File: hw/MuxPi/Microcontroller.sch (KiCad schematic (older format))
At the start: 34 parts, among them P1 DS1021-1*6SF1-1, SW1 DTSM-62N-V-B, SW2 DTSM-62N-V-B, U1 STM32F030C6T6, U3 OLED-AG-128032DY-Y (YELLOW), Y1 ABM3B-8.000MHZ-10-1-U-T

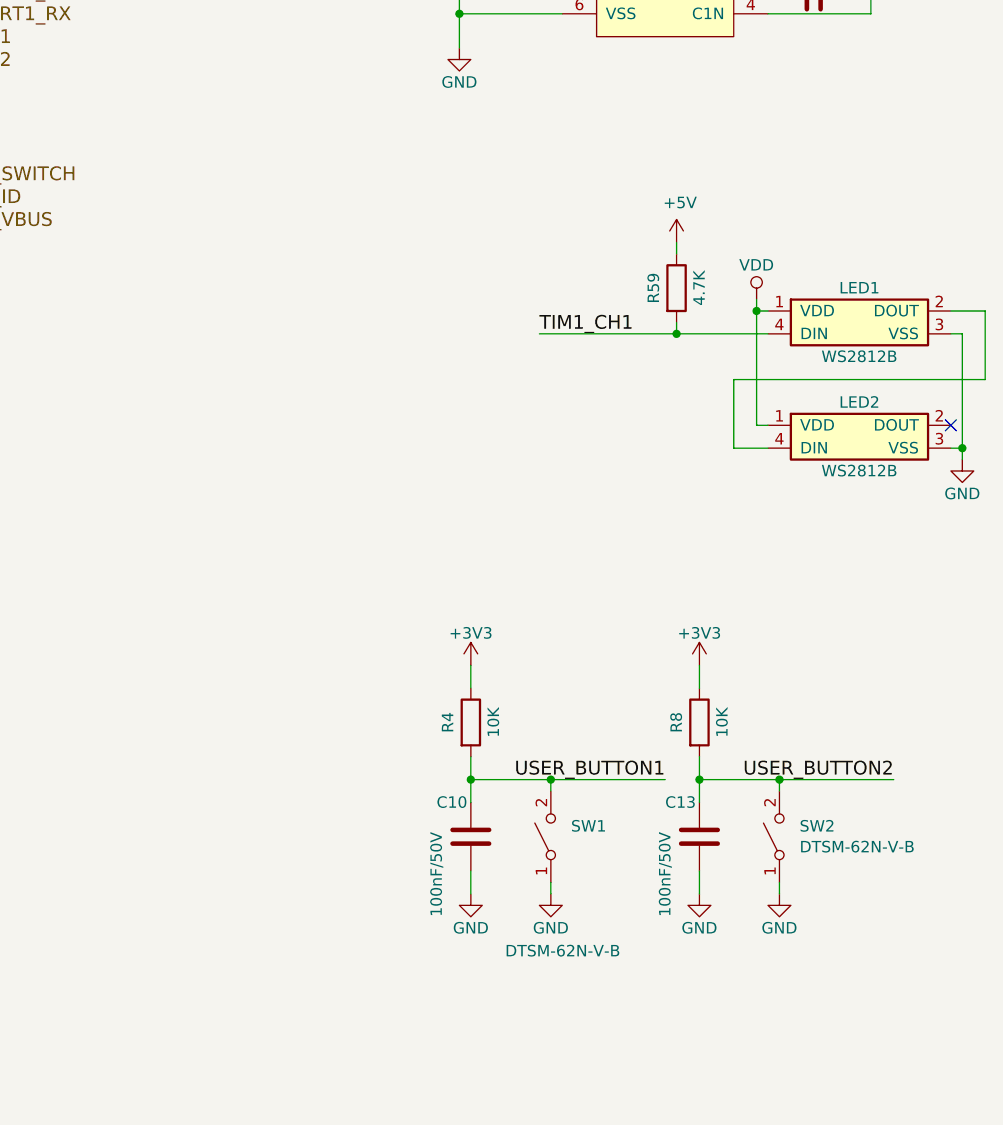
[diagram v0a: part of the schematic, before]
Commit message: Add detailed info to MuxPi electronic components
The additional information includes manufacturer names and
manufacturer symbols for all components except ceramic capacitors
and resistors. It allows to create BOM (Bill Of Materials) with
actual product names.

Change-Id: Id1c518bba60322d4b8b132ad14261806070abc27
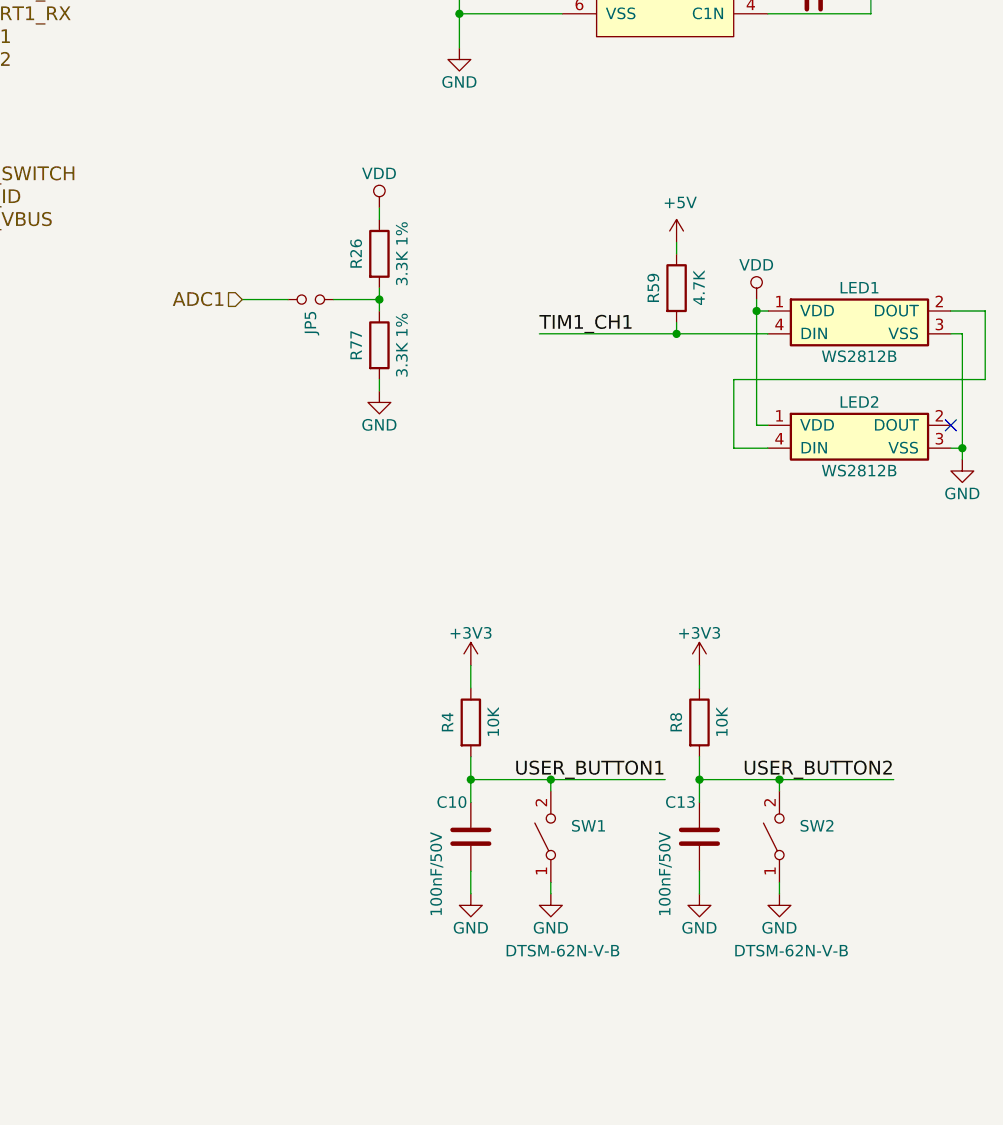
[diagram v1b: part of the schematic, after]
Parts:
- added JP5: Jumper_NO_Small, Pin_Headers:Pin_Header_Straight_1x02_Pitch2.54mm, symbol MuxPi:Jumper_NO_Small
- added R26, R77: 3.3K 1%, Resistors_SMD:R_0805, symbol MuxPi:R
- C75, C8: Manufacturer (none) -> KEMET; Symbol (none) -> T491A105K020AT
- JP4: Manufacturer (none) -> CONNFLY; Shop link (none) -> https://www.tme.eu/pl/details/zl201-02g/listwy-i-gniazda-ko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; Symbol (none) -> DS1021-1*2SF1-1
- LED1, LED2: Manufacturer (none) -> WORLDSEMI; Symbol (none) -> WS2812B
- P1: Shop link http://www.tme.eu/pl/details/zl201-06g/listwy-i-gniazda-kol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 -> (none)
- SW1, SW2: Manufacturer (none) -> DIPTRONICS; Symbol (none) -> DTSM-62N-V-B
- U1: Manufacturer (none) -> STMICROELECTRONICS; Symbol (none) -> STM32F030C6T6
- U3: Manufacturer (none) -> CHINA; Symbol (none) -> OLED-AG-128032DY-Y
- Y1: Manufacturer (none) -> ABRACON; Symbol (none) -> ABM3B-8.000MHZ-10-1-U-T
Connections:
- net ADC1: now also JP5.2
- net GND: now also R77.2
- net VDD: now also R26.1
- new net: JP5.1, R26.2, R77.1

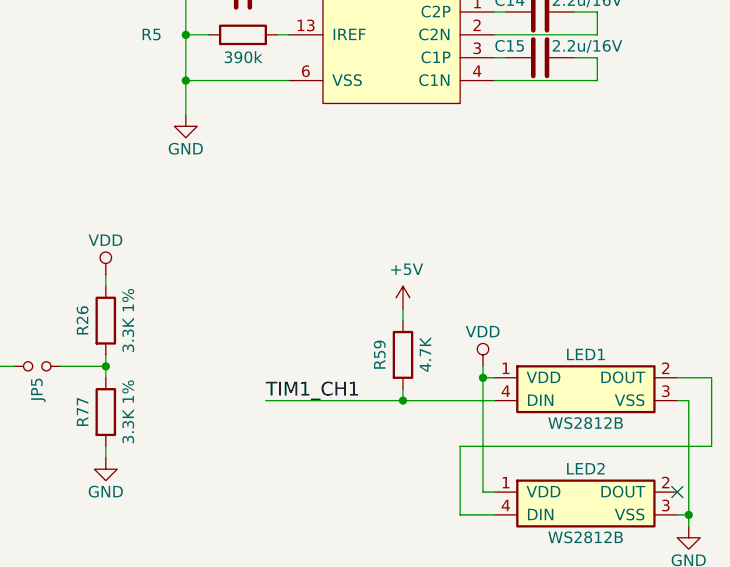
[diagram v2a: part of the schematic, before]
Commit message: Update hardware design to version 1.2
Change-Id: I36445887bfaa5fada88d8bf3915603605de47512
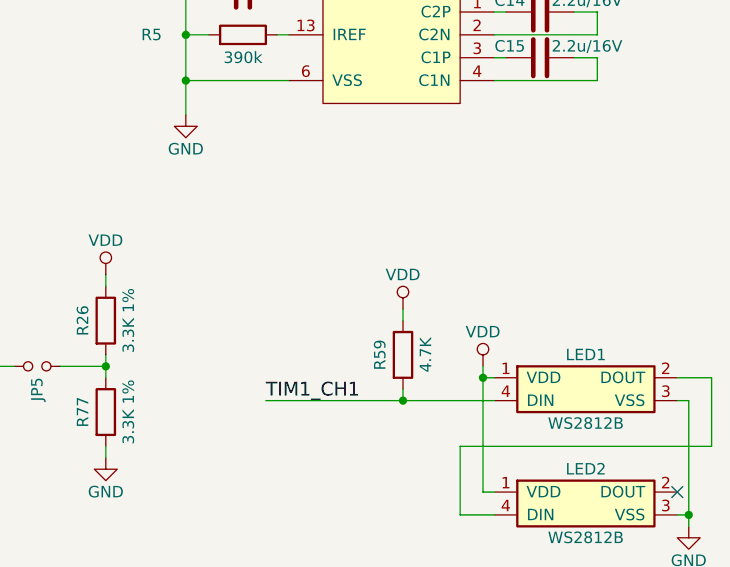
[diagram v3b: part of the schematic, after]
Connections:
- net +5V is gone; now on net VDD: R59.1
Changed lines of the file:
@@
 EESchema Schematic File Version 4
+LIBS:MuxPi-cache
 EELAYER 26 0
 EELAYER END
@@
 encoding utf-8
 Sheet 2 12
-Title ""
-Date ""
-Rev ""
-Comp ""
-Comment1 ""
-Comment2 ""
+Title "MuxPi"
+Date "2018-04-20"
+Rev "1.2"
+Comp "SRPOL"
+Comment1 "Author: Adam Malinowski <a.malinowsk2@partner.samsung.com>"
+Comment2 "Copyright (c) 2016 - 2018 Samsung Electronics Co., Ltd All Rights Reserved"
 Comment3 ""
 Comment4 ""
@@
 Wire Wire Line
 	9000 3500 9400 3500
-$Comp
-L MuxPi:+5V #PWR0202
-U 1 1 5A63A394
-P 9000 3100
-F 0 "#PWR0202" H 9000 2950 50  0001 C CNN
-F 1 "+5V" H 9015 3273 50  0000 C CNN
-F 2 "" H 9000 3100 50  0001 C CNN
-F 3 "" H 9000 3100 50  0001 C CNN
-	1    9000 3100
-	1    0    0    -1
-$EndComp
 Wire Wire Line
 	9000 3100 9000 3150
@@
 Wire Wire Line
 	7100 3350 7300 3350
+$Comp
+L MuxPi:VDD #PWR0202
+U 1 1 5AE48E8E
+P 9000 3100
+F 0 "#PWR0202" H 9000 2950 50  0001 C CNN
+F 1 "VDD" H 9000 3250 50  0000 C CNN
+F 2 "" H 9000 3100 60  0000 C CNN
+F 3 "" H 9000 3100 60  0000 C CNN
+	1    9000 3100
+	1    0    0    -1
+$EndComp
 $EndSCHEMATC

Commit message: Update  hardware design to version 1.4
Change-Id: I72a4381d8bec5616bc1cfe04dc8a5407141c77d5
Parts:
- removed JP4, JP5: Jumper_NO_Small, Pin_Headers:Pin_Header_Straight_1x02_Pitch2.54mm, symbol MuxPi:Jumper_NO_Small
- removed R2: 0R, Resistors_SMD:R_0805, symbol MuxPi:R
- removed R26, R77: 3.3K 1%, Resistors_SMD:R_0805, symbol MuxPi:R
- added C80: 10nF/50V, MuxPi:C_0805, symbol MuxPi:C
- added C83: 1uF/50V, MuxPi:C_0805, symbol MuxPi:C
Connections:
- net +3V3: now also C80.1, C83.1
- net GND: now also C80.2, C83.2
- net at U1.5 (OSC_IN): now also C7.1, Y1.1
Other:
- note added: "DNP"
- note added: "VDDA"
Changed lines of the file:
@@
 EESchema Schematic File Version 4
 LIBS:MuxPi-cache
-EELAYER 26 0
+EELAYER 29 0
 EELAYER END
 $Descr A4 11693 8268
@@
 Sheet 2 12
 Title "MuxPi"
-Date "2018-08-14"
-Rev "1.3"
+Date "2018-11-16"
+Rev "1.4"
 Comp "SRPOL"
 Comment1 "Author: Adam Malinowski <a.malinowsk2@partner.samsung.com>"
@@
 $EndComp
 $Comp
-L MuxPi:R R2
-U 1 1 58469A6E
-P 3150 3200
-F 0 "R2" V 3200 3000 50  0000 C CNN
-F 1 "0R" V 3250 3200 50  0000 C CNN
-F 2 "Resistors_SMD:R_0805" V 3080 3200 30  0001 C CNN
-F 3 "http://www.tme.eu/pl/Document/622e28308c06d160637f2b14751ba16b/Data%20Sheet%20CRCW_BCe3.pdf" H 3150 3200 30  0001 C CNN
-F 4 "http://www.tme.eu/pl/details/crcw08050000z0tabc/rezystory-smd-0805/vishay/" V 3150 3200 60  0001 C CNN "Shop link"
-	1    3150 3200
-	0    -1   -1   0
-$EndComp
-$Comp
 L MuxPi:R R3
 U 1 1 58469A75
@@
 	3050 7300 3050 7350
 Wire Wire Line
-	1150 3000 3750 3000
-Wire Wire Line
 	1150 1100 1150 1200
 Wire Wire Line
@@
 	2300 3200 2300 3500
 Wire Wire Line
-	2300 3200 3000 3200
-Wire Wire Line
 	2800 3300 2800 3500
 Wire Wire Line
@@
 	2700 3500 2800 3500
 Connection ~ 2800 3500
-Wire Wire Line
-	3300 3200 3750 3200
 Wire Wire Line
 	3600 3300 3750 3300
@@
 Wire Wire Line
 	9000 3100 9000 3150
-$Comp
-L MuxPi:GND #PWR0203
-U 1 1 5A64EB70
-P 1150 3350
-F 0 "#PWR0203" H 1150 3100 50  0001 C CNN
-F 1 "GND" H 1150 3200 50  0000 C CNN
-F 2 "" H 1150 3350 60  0000 C CNN
-F 3 "" H 1150 3350 60  0000 C CNN
-	1    1150 3350
-	-1   0    0    -1
-$EndComp
-Wire Wire Line
-	1150 3300 1150 3350
 Text HLabel 1050 3000 0    60   Input ~ 0
 PI_GPIO_1
-Wire Wire Line
-	1050 3000 1150 3000
-Wire Wire Line
-	1150 3000 1150 3100
-Connection ~ 1150 3000
-$Comp
-L MuxPi:Jumper_NO_Small JP4
-U 1 1 5A8C7652
-P 1150 3200
-F 0 "JP4" V 1150 3248 50  0000 L CNN
-F 1 "Jumper_NO_Small" V 1195 3248 50  0001 L CNN
-F 2 "Pin_Headers:Pin_Header_Straight_1x02_Pitch2.54mm" H 1150 3200 50  0001 C CNN
-F 3 "https://www.tme.eu/pl/Document/cc301e58a5da78cb543a94b5a5b7f06a/DS1021.pdf" H 1150 3200 50  0001 C CNN
-F 4 "https://www.tme.eu/pl/details/zl201-02g/listwy-i-gniazda-kolkowe/connfly/ds1021-1_2sf1-1/" V 1150 3200 50  0001 C CNN "Shop link"
-F 5 "CONNFLY" V 1150 3200 50  0001 C CNN "Manufacturer"
-F 6 "DS1021-1*2SF1-1" V 1150 3200 50  0001 C CNN "Symbol"
-	1    1150 3200
-	0    1    1    0
-$EndComp
 $Comp
 L MuxPi:CP C75
@@
 $EndComp
 $Comp
-L MuxPi:R R26
-U 1 1 5A8AD04E
-P 7700 3150
-F 0 "R26" V 7600 3150 50  0000 C CNN
-F 1 "3.3K 1%" V 7800 3150 50  0000 C CNN
-F 2 "Resistors_SMD:R_0805" V 7630 3150 30  0001 C CNN
-F 3 "https://www.tme.eu/pl/Document/7b8fed8c112f8a94930279c22c957f7f/rc0805yageo.pdf" H 7700 3150 30  0001 C CNN
-F 4 "https://www.tme.eu/pl/details/rc0805fr-073k3/rezystory-smd-0805/yageo/rc0805fr-073k3l/" V 7700 3150 60  0001 C CNN "Shop link"
-	1    7700 3150
-	1    0    0    -1
-$EndComp
-$Comp
-L MuxPi:R R77
-U 1 1 5A8AD056
-P 7700 3550
-F 0 "R77" V 7600 3550 50  0000 C CNN
-F 1 "3.3K 1%" V 7800 3550 50  0000 C CNN
-F 2 "Resistors_SMD:R_0805" V 7630 3550 30  0001 C CNN
-F 3 "https://www.tme.eu/pl/Document/7b8fed8c112f8a94930279c22c957f7f/rc0805yageo.pdf" H 7700 3550 30  0001 C CNN
-F 4 "https://www.tme.eu/pl/details/rc0805fr-073k3/rezystory-smd-0805/yageo/rc0805fr-073k3l/" V 7700 3550 60  0001 C CNN "Shop link"
-	1    7700 3550
-	1    0    0    -1
-$EndComp
-Wire Wire Line
-	7700 3300 7700 3350
-$Comp
-L MuxPi:Jumper_NO_Small JP5
-U 1 1 5A8B4A8C
-P 7400 3350
-F 0 "JP5" V 7400 3398 50  0000 L CNN
-F 1 "Jumper_NO_Small" V 7445 3398 50  0001 L CNN
-F 2 "Pin_Headers:Pin_Header_Straight_1x02_Pitch2.54mm" H 7400 3350 50  0001 C CNN
-F 3 "https://www.tme.eu/pl/Document/cc301e58a5da78cb543a94b5a5b7f06a/DS1021.pdf" H 7400 3350 50  0001 C CNN
-F 4 "https://www.tme.eu/pl/details/zl201-02g/listwy-i-gniazda-kolkowe/connfly/ds1021-1_2sf1-1/" V 7400 3350 50  0001 C CNN "Shop link"
-F 5 "CONNFLY" V 7400 3350 50  0001 C CNN "Manufacturer"
-F 6 "DS1021-1*2SF1-1" V 7400 3350 50  0001 C CNN "Symbol"
-	1    7400 3350
-	-1   0    0    1
-$EndComp
-Wire Wire Line
-	7500 3350 7700 3350
-Connection ~ 7700 3350
-Wire Wire Line
-	7700 3350 7700 3400
-$Comp
-L MuxPi:VDD #PWR086
-U 1 1 5A8BBDA8
-P 7700 2950
-F 0 "#PWR086" H 7700 2800 50  0001 C CNN
-F 1 "VDD" H 7700 3100 50  0000 C CNN
-F 2 "" H 7700 2950 60  0000 C CNN
-F 3 "" H 7700 2950 60  0000 C CNN
-	1    7700 2950
-	1    0    0    -1
-$EndComp
-Wire Wire Line
-	7700 2950 7700 3000
-$Comp
-L MuxPi:GND #PWR0197
-U 1 1 5A8C310E
-P 7700 3750
-F 0 "#PWR0197" H 7700 3500 50  0001 C CNN
-F 1 "GND" H 7700 3600 50  0000 C CNN
-F 2 "" H 7700 3750 60  0000 C CNN
-F 3 "" H 7700 3750 60  0000 C CNN
-	1    7700 3750
-	1    0    0    -1
-$EndComp
-Wire Wire Line
-	7700 3700 7700 3750
-Text HLabel 7100 3350 0    60   Input ~ 0
-ADC1
-Wire Wire Line
-	7100 3350 7300 3350
-$Comp
 L MuxPi:VDD #PWR0202
 U 1 1 5AE48E8E
@@
 	1    0    0    -1
 $EndComp
+Wire Wire Line
+	1050 3000 3750 3000
+Wire Wire Line
+	2300 3200 3750 3200
+$Comp
+L MuxPi:GND #PWR0194
+U 1 1 5C3ABA0A
+P 4750 7350
+F 0 "#PWR0194" H 4750 7100 50  0001 C CNN
+F 1 "GND" H 4750 7200 50  0000 C CNN
+F 2 "" H 4750 7350 60  0000 C CNN
+F 3 "" H 4750 7350 60  0000 C CNN
+	1    4750 7350
+	1    0    0    -1
+$EndComp
+$Comp
+L MuxPi:+3V3 #PWR086
+U 1 1 5C3ABA14
+P 4750 6950
+F 0 "#PWR086" H 4750 6800 50  0001 C CNN
+F 1 "+3V3" H 4750 7090 50  0000 C CNN
+F 2 "" H 4750 6950 60  0000 C CNN
+F 3 "" H 4750 6950 60  0000 C CNN
+	1    4750 6950
+	1    0    0    -1
+$EndComp
+Wire Wire Line
+	4750 6950 4750 7000
+Wire Wire Line
+	4750 7300 4750 7350
+$Comp
+L MuxPi:C C80
+U 1 1 5C3ABA21
+P 4750 7150
+F 0 "C80" H 4600 7300 50  0000 L CNN
+F 1 "10nF/50V" V 4600 6800 50  0000 L CNN
+F 2 "MuxPi:C_0805" H 4788 7000 50  0001 C CNN
+F 3 "https://www.tme.eu/pl/Document/3d8d32d2b2532d751869808a982e3e31/AVX_FlexitermMLCC.pdf" H 4750 7150 50  0001 C CNN
+F 4 "https://www.tme.eu/pl/details/08051c103k4z2a/kondensatory-mlcc-smd-0805/avx/" H 4750 7150 60  0001 C CNN "Shop link"
+	1    4750 7150
+	1    0    0    -1
+$EndComp
+$Comp
+L MuxPi:GND #PWR0220
+U 1 1 5C3B2C79
+P 5050 7350
+F 0 "#PWR0220" H 5050 7100 50  0001 C CNN
+F 1 "GND" H 5050 7200 50  0000 C CNN
+F 2 "" H 5050 7350 60  0000 C CNN
+F 3 "" H 5050 7350 60  0000 C CNN
+	1    5050 7350
+	1    0    0    -1
+$EndComp
+$Comp
+L MuxPi:+3V3 #PWR0211
+U 1 1 5C3B2C83
+P 5050 6950
+F 0 "#PWR0211" H 5050 6800 50  0001 C CNN
+F 1 "+3V3" H 5050 7090 50  0000 C CNN
+F 2 "" H 5050 6950 60  0000 C CNN
+F 3 "" H 5050 6950 60  0000 C CNN
+	1    5050 6950
+	1    0    0    -1
+$EndComp
+Wire Wire Line
+	5050 6950 5050 7000
+Wire Wire Line
+	5050 7300 5050 7350
+$Comp
+L MuxPi:C C83
+U 1 1 5C3B2C90
+P 5050 7150
+F 0 "C83" H 4900 7300 50  0000 L CNN
+F 1 "1uF/50V" V 4900 6800 50  0000 L CNN
+F 2 "MuxPi:C_0805" H 5088 7000 50  0001 C CNN
+F 3 "https://www.tme.eu/pl/Document/6a5ad7ac81542ad65ce1ca82bcd21ffa/vjw1bcbascomseries.pdf" H 5050 7150 50  0001 C CNN
+F 4 "https://www.tme.eu/pl/details/vj0805y105kxxtw1bc/kondensatory-mlcc-smd-0805/vishay/" H 5050 7150 60  0001 C CNN "Shop link"
+	1    5050 7150
+	1    0    0    -1
+$EndComp
+Text Notes 4800 6650 0    60   ~ 0
+VDDA
+Text Notes 750  2750 0    60   ~ 12
+DNP
 $EndSCHEMATC
